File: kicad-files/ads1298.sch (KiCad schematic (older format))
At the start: 1 part

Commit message: add power decoupling caps to ADS
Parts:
- added C? (x8): 100nF, symbol C
- added C? (x9): 1uF, symbol C
- added C?: 10uF, symbol C
- added C?: 22uF, symbol C
- added C?: 100pF, symbol C
- added C?: 10nF, symbol C
- added R?: 392k, symbol R
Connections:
- net labels added: ADS_AGND, AGND, DGND, DVDD, RLDOUT
- net labels removed: ADS_AVSS, AVSS, VSSA
- wire segments 39 -> 145
- no-connect marks 1 -> 2
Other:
- note added: "AVDD1\nStar Power"
- moved on the sheet: U?

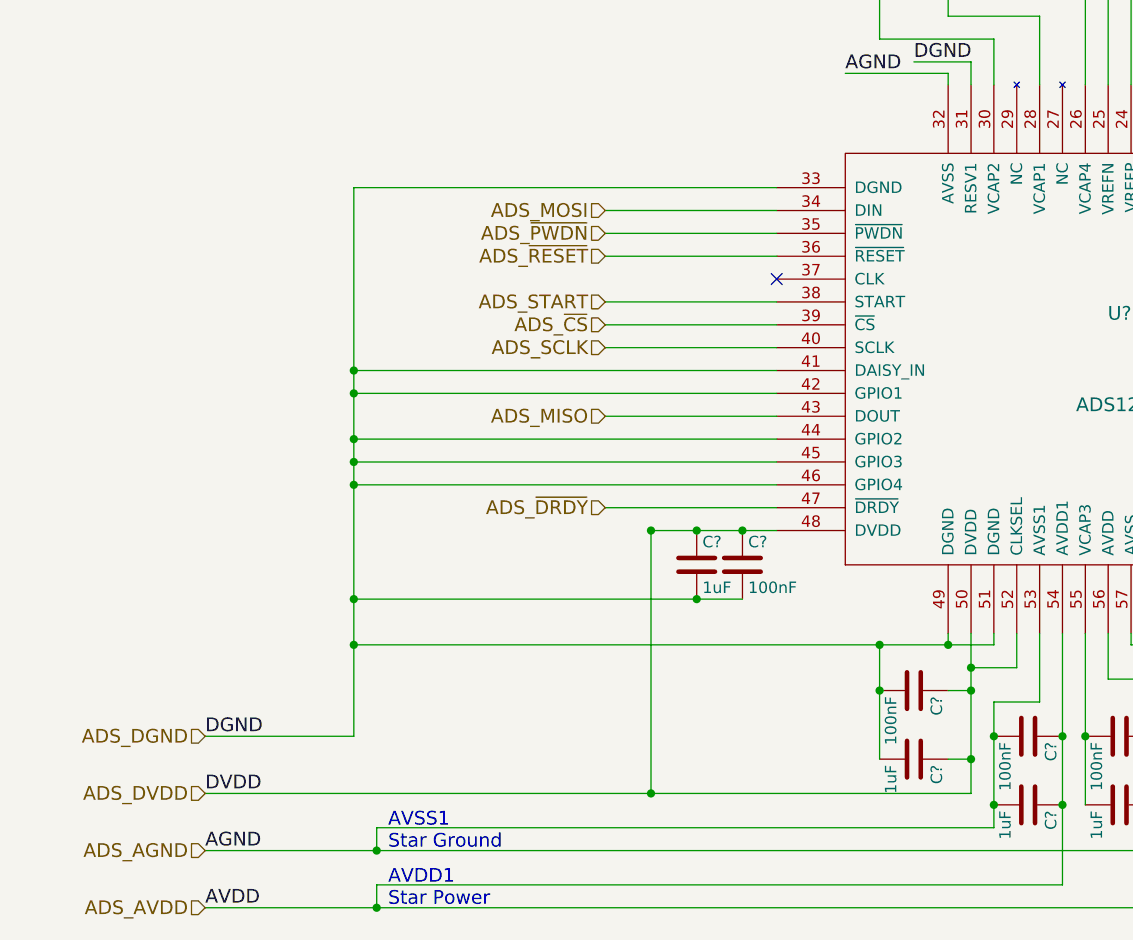
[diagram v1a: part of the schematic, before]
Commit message: ads schematic cleanup and add source termination
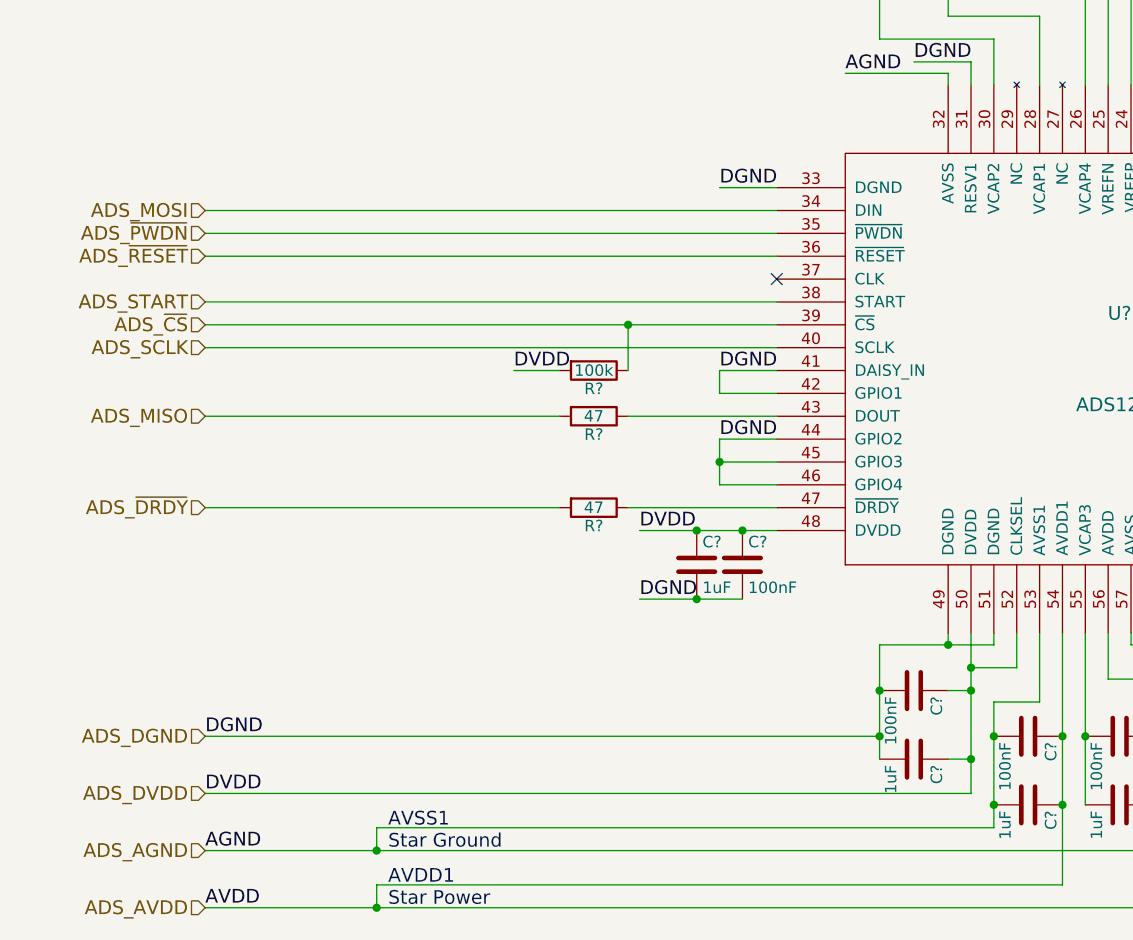
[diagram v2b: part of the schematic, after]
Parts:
- added R? (x2): 47, symbol R
- added R?: 100k, symbol R
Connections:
- net ADS_DVDD: now also R?.2
- net ADS_MISO: now also R?.2; no longer U?.43 (DOUT)
- net ADS_~CS~: now also R?.1
- net ADS_~DRDY~: now also R?.2; no longer U?.47 (~DRDY~)
- new net: R?.1, U?.43 (DOUT)
- new net: R?.1, U?.47 (~DRDY~)

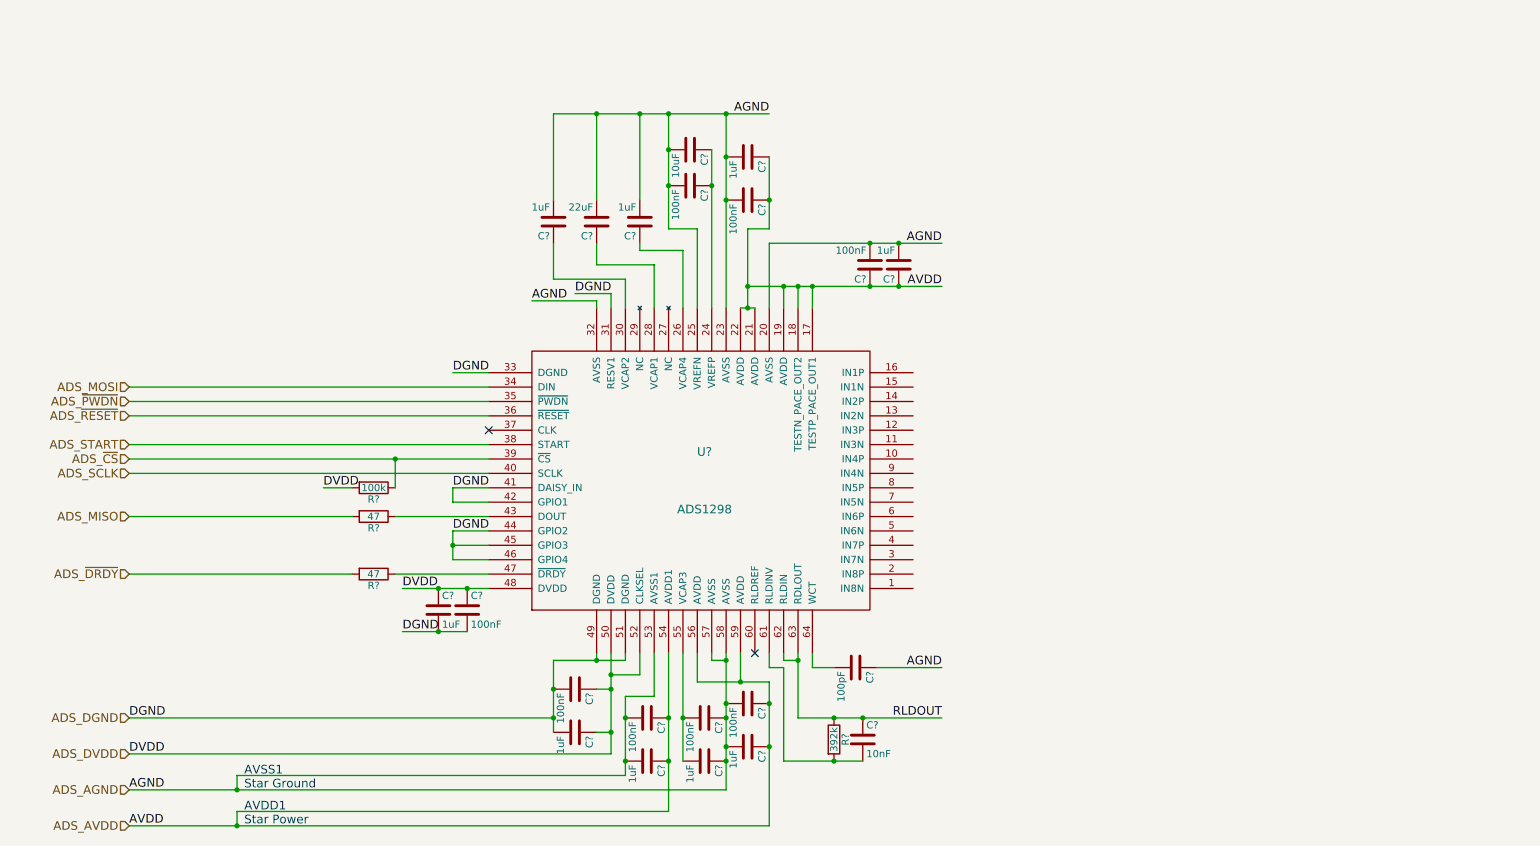
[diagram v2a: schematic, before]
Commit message: add anti-aliasing filters
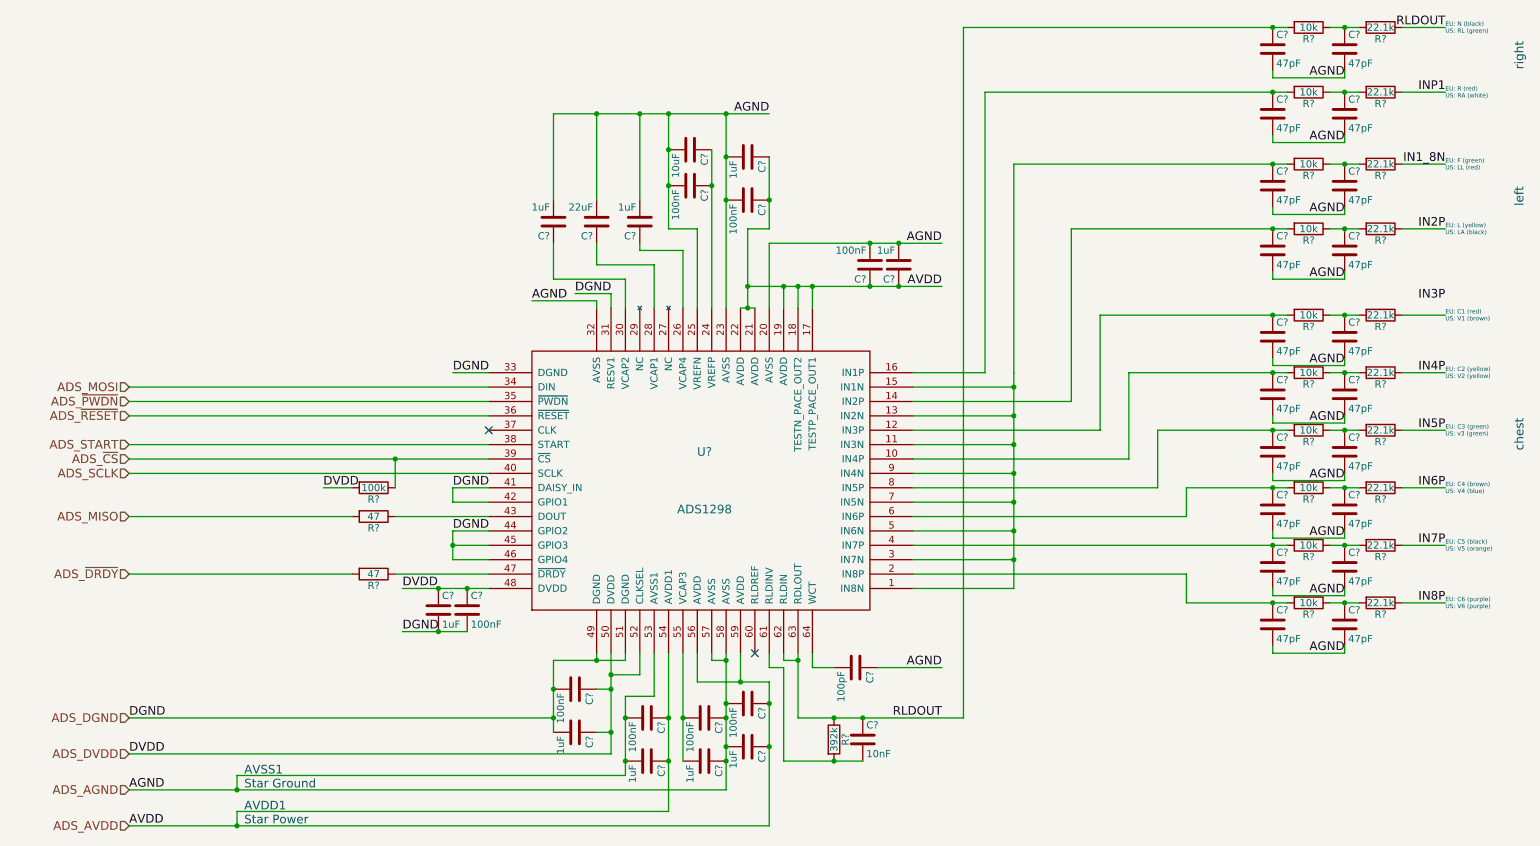
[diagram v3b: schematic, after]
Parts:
- added C? (x20): 47pF, symbol C
- added R? (x10): 22.1k, symbol R
- added R? (x10): 10k, symbol R
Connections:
- net ADS_AGND: now also C?.2, C?.2, C?.2, C?.2, C?.2, C?.2, C?.2, C?.2, C?.2, C?.2, C?.2, C?.2, C?.2, C?.2, C?.2, C?.2, C?.2, C?.2, C?.2, C?.2
- net RLDOUT: now also C?.1, R?.1, R?.2
- net at U?.1 (IN8N): now also U?.11 (IN3N), U?.13 (IN2N), U?.15 (IN1N), U?.3 (IN7N), U?.5 (IN6N), U?.7 (IN5N), U?.9 (IN4N), C?.1, R?.2
- net at U?.10 (IN4P): now also C?.1, R?.2
- net at U?.12 (IN3P): now also C?.1, R?.2
- net at U?.14 (IN2P): now also C?.1, R?.2
- net at U?.16 (IN1P): now also C?.1, R?.2
- net at U?.2 (IN8P): now also C?.1, R?.2
- net at U?.4 (IN7P): now also C?.1, R?.2
- net at U?.6 (IN6P): now also C?.1, R?.2
- net at U?.8 (IN5P): now also C?.1, R?.2
- new net: C?.1, R?.1, R?.2 (x10)
- new net IN1_8N: R?.1
- new net IN2P: R?.1
- new net IN4P: R?.1
- new net IN5P: R?.1
- new net IN6P: R?.1
- new net IN7P: R?.1
- new net IN8P: R?.1
- new net INP1: R?.1
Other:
- note added: "EU: C1 (red)\nUS: V1 (brown)"
- note added: "EU: C2 (yellow)\nUS: V2 (yellow)"
- note added: "EU: C3 (green)\nUS: v3 (green)"
- note added: "EU: C4 (brown)\nUS: V4 (blue)"
- note added: "EU: C5 (black)\nUS: V5 (orange)"
- note added: "EU: C6 (purple)\nUS: V6 (purple)"
- note added: "EU: F (green)\nUS: LL (red)"
- note added: "EU: L (yellow)\nUS: LA (black)"
- note added: "EU: N (black)\nUS: RL (green)"
- note added: "EU: R (red)\nUS: RA (white)"
- note added: "chest"
- note added: "left"
- note added: "right"

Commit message: simplify anti-aliasing filter
new low-pass filter cuts off at about 6.6KHz

>>> 1/(2 * math.pi * 51e3 * 470e-12)
6639.755656733221
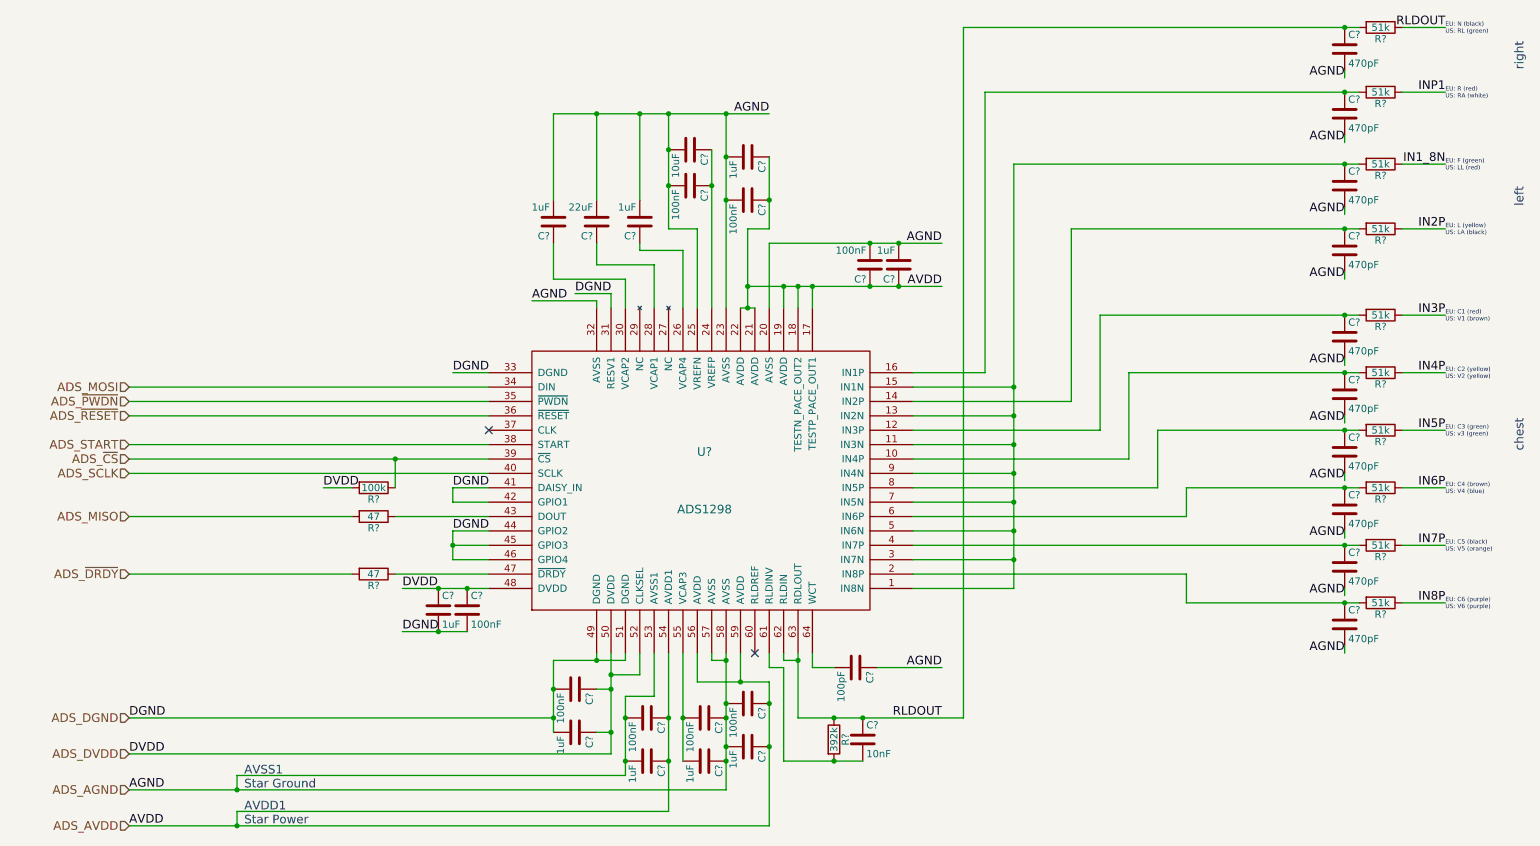
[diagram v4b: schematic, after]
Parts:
- removed C? (x10): 47pF, symbol C
- removed R? (x10): 10k, symbol R
- C? (x10): value 47pF -> 470pF
- R? (x10): value 22.1k -> 51k
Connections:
- net IN3P: now also R?.1
- net RLDOUT: now also C?.1, R?.2
- net at U?.1 (IN8N), U?.11 (IN3N), U?.13 (IN2N)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: now also C?.1, R?.2
- net at U?.10 (IN4P): now also C?.1, R?.2
- net at U?.12 (IN3P): now also C?.1, R?.2
- net at U?.14 (IN2P): now also C?.1, R?.2
- net at U?.16 (IN1P): now also C?.1, R?.2
- net at U?.2 (IN8P): now also C?.1, R?.2
- net at U?.4 (IN7P): now also C?.1, R?.2
- net at U?.6 (IN6P): now also C?.1, R?.2
- net at U?.8 (IN5P): now also C?.1, R?.2
